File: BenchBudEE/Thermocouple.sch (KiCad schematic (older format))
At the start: 14 parts

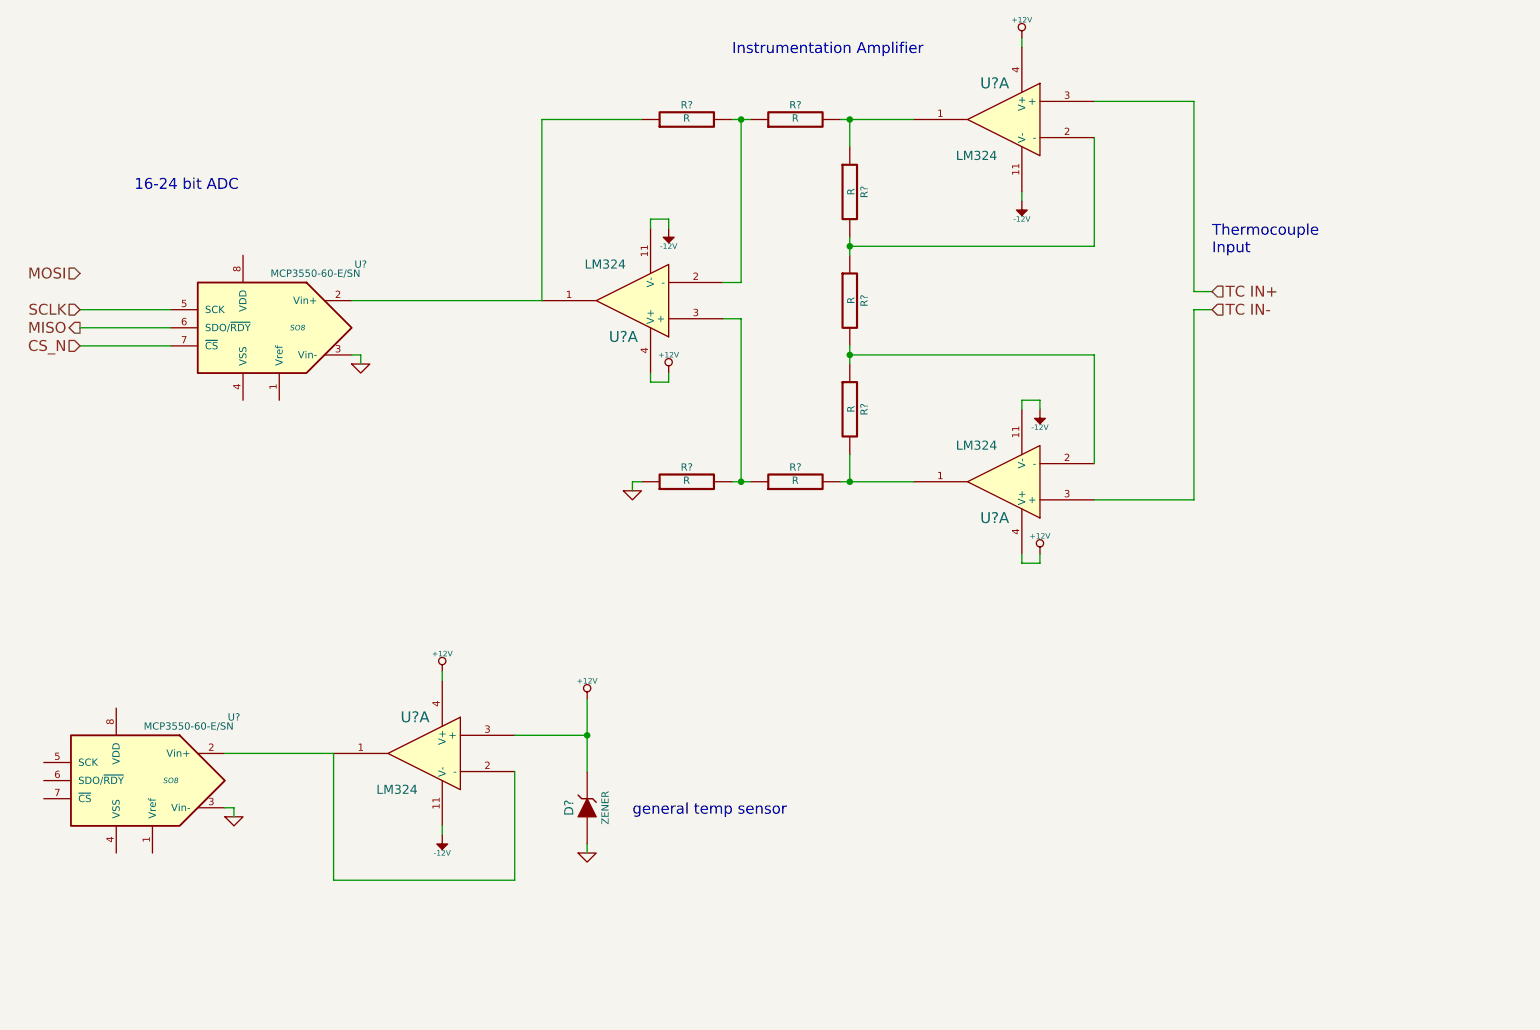
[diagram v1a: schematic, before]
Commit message: Completing schematics from week 3 videos.
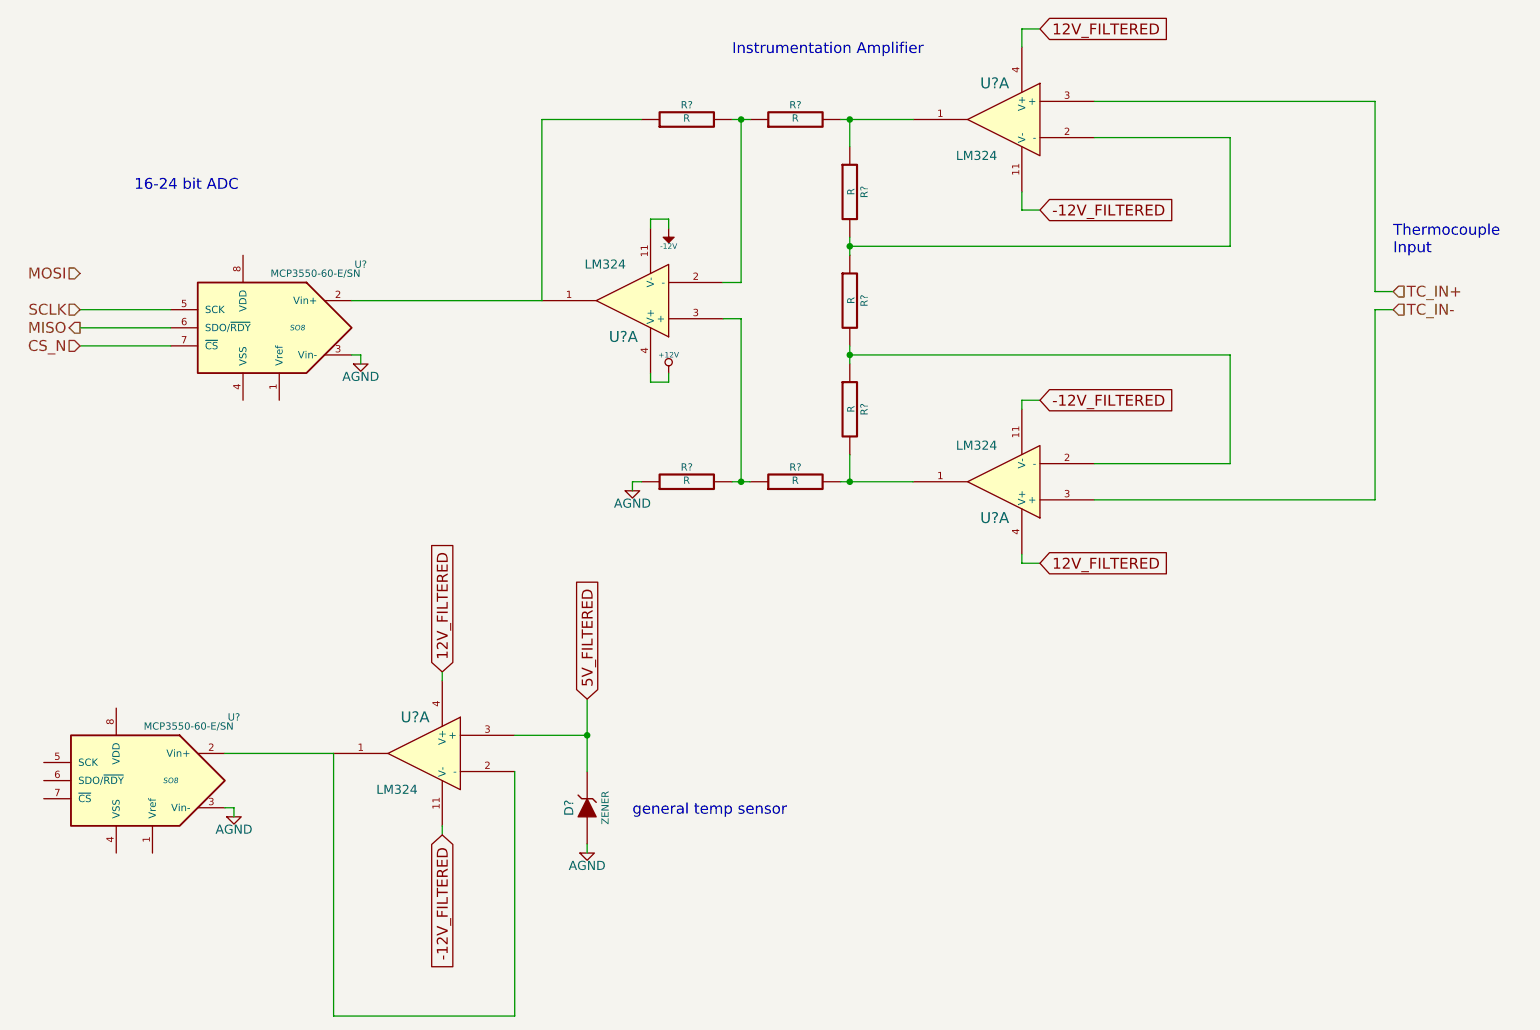
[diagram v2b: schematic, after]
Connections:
- net +12V: no longer D?.2 (K), U?.3 (+), U?.4 (V+), U?.4 (V+), U?.4 (V+)
- net -12V: no longer U?.11 (V-), U?.11 (V-), U?.11 (V-)
- net GND renamed AGND
- net TC IN+ renamed TC_IN+
- net TC IN- renamed TC_IN-
- new net -12V_FILTERED: U?.11 (V-), U?.11 (V-), U?.11 (V-)
- new net 12V_FILTERED: U?.4 (V+), U?.4 (V+), U?.4 (V+)
- new net 5V_FILTERED: D?.2 (K), U?.3 (+)
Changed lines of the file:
@@
 LIBS:relay_spdt
 LIBS:5566-20A
+LIBS:AP5726
+LIBS:arduino
 LIBS:BenchBudEE-cache
 EELAYER 27 0
@@
 $Descr A4 11693 8268
 encoding utf-8
-Sheet 3 9
+Sheet 2 9
 Title ""
-Date "13 feb 2014"
+Date "24 feb 2014"
 Rev ""
 Comp ""
@@
 Comment4 ""
 $EndDescr
-Text HLabel 8750 2750 2    60   Input ~ 0
-TC IN+
-Text HLabel 8750 2850 2    60   Input ~ 0
-TC IN-
+Text HLabel 9750 2750 2    60   Input ~ 0
+TC_IN+
+Text HLabel 9750 2850 2    60   Input ~ 0
+TC_IN-
 Text HLabel 2500 2650 0    60   Input ~ 0
 MOSI
@@
 $Comp
 L LM324 U?
-U 1 1 52F7EF65
-P 7600 3800
-F 0 "U?" H 7650 4000 60  0000 C CNN
-F 1 "LM324" H 7750 3600 50  0000 C CNN
-F 2 "" H 7600 3800 60  0000 C CNN
-F 3 "" H 7600 3800 60  0000 C CNN
-	1    7600 3800
-	-1   0    0    1
-$EndComp
-$Comp
-L LM324 U?
 U 1 1 52F7EF74
 P 5550 2800
@@
 $EndComp
 $Comp
-L -12V #PWR?
-U 1 1 52F7F282
-P 7800 3400
-F 0 "#PWR?" H 7800 3530 20  0001 C CNN
-F 1 "-12V" H 7800 3500 30  0000 C CNN
-F 2 "" H 7800 3400 60  0000 C CNN
-F 3 "" H 7800 3400 60  0000 C CNN
-	1    7800 3400
-	-1   0    0    1
-$EndComp
-$Comp
-L -12V #PWR?
-U 1 1 52F7F291
-P 7700 2250
-F 0 "#PWR?" H 7700 2380 20  0001 C CNN
-F 1 "-12V" H 7700 2350 30  0000 C CNN
-F 2 "" H 7700 2250 60  0000 C CNN
-F 3 "" H 7700 2250 60  0000 C CNN
-	1    7700 2250
-	-1   0    0    1
-$EndComp
-$Comp
 L +12V #PWR?
 U 1 1 52F7F33B
@@
 F 3 "" H 5750 3200 60  0000 C CNN
 	1    5750 3200
-	1    0    0    -1
-$EndComp
-$Comp
-L +12V #PWR?
-U 1 1 52F7F34A
-P 7800 4200
-F 0 "#PWR?" H 7800 4150 20  0001 C CNN
-F 1 "+12V" H 7800 4300 30  0000 C CNN
-F 2 "" H 7800 4200 60  0000 C CNN
-F 3 "" H 7800 4200 60  0000 C CNN
-	1    7800 4200
-	1    0    0    -1
-$EndComp
-$Comp
-L +12V #PWR?
-U 1 1 52F7F359
-P 7700 1350
-F 0 "#PWR?" H 7700 1300 20  0001 C CNN
-F 1 "+12V" H 7700 1450 30  0000 C CNN
-F 2 "" H 7700 1350 60  0000 C CNN
-F 3 "" H 7700 1350 60  0000 C CNN
-	1    7700 1350
-	1    0    0    -1
-$EndComp
-$Comp
-L GND #PWR?
-U 1 1 52F7F3EE
-P 5550 3850
-F 0 "#PWR?" H 5550 3850 30  0001 C CNN
-F 1 "GND" H 5550 3780 30  0001 C CNN
-F 2 "" H 5550 3850 60  0000 C CNN
-F 3 "" H 5550 3850 60  0000 C CNN
-	1    5550 3850
 	1    0    0    -1
 $EndComp
@@
 $EndComp
 $Comp
-L GND #PWR?
-U 1 1 52F7F4AB
-P 4050 3150
-F 0 "#PWR?" H 4050 3150 30  0001 C CNN
-F 1 "GND" H 4050 3080 30  0001 C CNN
-F 2 "" H 4050 3150 60  0000 C CNN
-F 3 "" H 4050 3150 60  0000 C CNN
-	1    4050 3150
-	1    0    0    -1
-$EndComp
-$Comp
 L MCP3550-60-E/SN U?
 U 1 1 52F7F58D
@@
 	0    -1   -1   0
 $EndComp
-$Comp
-L GND #PWR?
-U 1 1 52F7F5D7
-P 5300 5850
-F 0 "#PWR?" H 5300 5850 30  0001 C CNN
-F 1 "GND" H 5300 5780 30  0001 C CNN
-F 2 "" H 5300 5850 60  0000 C CNN
-F 3 "" H 5300 5850 60  0000 C CNN
-	1    5300 5850
-	1    0    0    -1
-$EndComp
-$Comp
-L +12V #PWR?
-U 1 1 52F7F612
-P 5300 5000
-F 0 "#PWR?" H 5300 4950 20  0001 C CNN
-F 1 "+12V" H 5300 5100 30  0000 C CNN
-F 2 "" H 5300 5000 60  0000 C CNN
-F 3 "" H 5300 5000 60  0000 C CNN
-	1    5300 5000
-	1    0    0    -1
-$EndComp
-$Comp
-L +12V #PWR?
-U 1 1 52F7F627
-P 4500 4850
-F 0 "#PWR?" H 4500 4800 20  0001 C CNN
-F 1 "+12V" H 4500 4950 30  0000 C CNN
-F 2 "" H 4500 4850 60  0000 C CNN
-F 3 "" H 4500 4850 60  0000 C CNN
-	1    4500 4850
-	1    0    0    -1
-$EndComp
-$Comp
-L -12V #PWR?
-U 1 1 52F7F62D
-P 4500 5750
-F 0 "#PWR?" H 4500 5880 20  0001 C CNN
-F 1 "-12V" H 4500 5850 30  0000 C CNN
-F 2 "" H 4500 5750 60  0000 C CNN
-F 3 "" H 4500 5750 60  0000 C CNN
-	1    4500 5750
-	-1   0    0    1
-$EndComp
 Wire Wire Line
 	6750 2450 6750 2550
@@
 Wire Wire Line
 	6750 3800 6750 3650
-Wire Wire Line
-	6750 3100 8100 3100
-Wire Wire Line
-	8100 3100 8100 3700
 Connection ~ 6750 3100
 Wire Wire Line
-	6750 2500 8100 2500
-Wire Wire Line
-	8100 2500 8100 1900
+	6750 2500 8850 2500
 Connection ~ 6750 2500
 Wire Wire Line
-	8750 2750 8650 2750
-Wire Wire Line
-	8650 2750 8650 1700
-Wire Wire Line
-	8650 1700 8100 1700
-Wire Wire Line
-	8750 2850 8650 2850
-Wire Wire Line
-	8650 2850 8650 3900
-Wire Wire Line
-	8650 3900 8100 3900
+	9750 2750 9650 2750
+Wire Wire Line
+	9650 2750 9650 1700
+Wire Wire Line
+	9650 1700 8100 1700
+Wire Wire Line
+	9750 2850 9650 2850
+Wire Wire Line
+	9650 2850 9650 3900
+Wire Wire Line
+	9650 3900 8100 3900
 Connection ~ 6750 1800
 Connection ~ 6750 3800
@@
 	5750 2350 5750 2400
 Wire Wire Line
-	7700 2200 7700 2250
-Wire Wire Line
 	7700 3400 7700 3350
 Wire Wire Line
 	7700 3350 7800 3350
 Wire Wire Line
-	7800 3350 7800 3400
-Wire Wire Line
-	7700 1350 7700 1400
+	7700 1300 7700 1400
 Wire Wire Line
 	7700 4200 7700 4250
@@
 	7700 4250 7800 4250
 Wire Wire Line
-	7800 4250 7800 4200
-Wire Wire Line
 	5650 3200 5650 3250
 Wire Wire Line
@@
 	5300 5000 5300 5400
 Wire Wire Line
-	3900 5300 3900 6000
-Wire Wire Line
-	3900 6000 4900 6000
-Wire Wire Line
-	4900 6000 4900 5400
+	3900 5300 3900 6750
+Wire Wire Line
+	4900 5400 4900 6750
 Wire Wire Line
 	4900 5200 5300 5200
@@
 Wire Wire Line
 	3900 5300 3300 5300
-$Comp
-L GND #PWR?
-U 1 1 52F7F813
-P 3350 5650
-F 0 "#PWR?" H 3350 5650 30  0001 C CNN
-F 1 "GND" H 3350 5580 30  0001 C CNN
-F 2 "" H 3350 5650 60  0000 C CNN
-F 3 "" H 3350 5650 60  0000 C CNN
-	1    3350 5650
-	1    0    0    -1
-$EndComp
 Wire Wire Line
 	3300 5600 3350 5600
@@
 Text Notes 5550 5650 0    60   ~ 0
 general temp sensor
-Text Notes 8750 2550 0    60   ~ 0
+Text Notes 9750 2550 0    60   ~ 0
 Thermocouple\nInput
 Text Notes 6100 1450 0    60   ~ 0
@@
 Text Notes 2800 2200 0    60   ~ 0
 16-24 bit ADC
+$Comp
+L AGND #PWR?
+U 1 1 53098A6F
+P 3350 5650
+F 0 "#PWR?" H 3350 5650 40  0001 C CNN
+F 1 "AGND" H 3350 5580 50  0000 C CNN
+F 2 "" H 3350 5650 60  0000 C CNN
+F 3 "" H 3350 5650 60  0000 C CNN
+	1    3350 5650
+	1    0    0    -1
+$EndComp
+$Comp
+L AGND #PWR?
+U 1 1 53098A7E
+P 5300 5850
+F 0 "#PWR?" H 5300 5850 40  0001 C CNN
+F 1 "AGND" H 5300 5780 50  0000 C CNN
+F 2 "" H 5300 5850 60  0000 C CNN
+F 3 "" H 5300 5850 60  0000 C CNN
+	1    5300 5850
+	1    0    0    -1
+$EndComp
+Text GLabel 5300 5000 1    60   Input ~ 0
+5V_FILTERED
+Text GLabel 4500 4850 1    60   Input ~ 0
+12V_FILTERED
+Text GLabel 4500 5750 3    60   Input ~ 0
+-12V_FILTERED
+Wire Wire Line
+	4900 6750 3900 6750
+$Comp
+L LM324 U?
+U 1 1 52F7EF65
+P 7600 3800
+F 0 "U?" H 7650 4000 60  0000 C CNN
+F 1 "LM324" H 7750 3600 50  0000 C CNN
+F 2 "" H 7600 3800 60  0000 C CNN
+F 3 "" H 7600 3800 60  0000 C CNN
+	1    7600 3800
+	-1   0    0    1
+$EndComp
+Text GLabel 7800 4250 2    60   Input ~ 0
+12V_FILTERED
+$Comp
+L AGND #PWR?
+U 1 1 53098ACE
+P 5550 3850
+F 0 "#PWR?" H 5550 3850 40  0001 C CNN
+F 1 "AGND" H 5550 3780 50  0000 C CNN
+F 2 "" H 5550 3850 60  0000 C CNN
+F 3 "" H 5550 3850 60  0000 C CNN
+	1    5550 3850
+	1    0    0    -1
+$EndComp
+$Comp
+L AGND #PWR?
+U 1 1 53098ADD
+P 4050 3150
+F 0 "#PWR?" H 4050 3150 40  0001 C CNN
+F 1 "AGND" H 4050 3080 50  0000 C CNN
+F 2 "" H 4050 3150 60  0000 C CNN
+F 3 "" H 4050 3150 60  0000 C CNN
+	1    4050 3150
+	1    0    0    -1
+$EndComp
+Text GLabel 7800 3350 2    60   Input ~ 0
+-12V_FILTERED
+Text GLabel 7800 2300 2    60   Input ~ 0
+-12V_FILTERED
+Wire Wire Line
+	7800 2300 7700 2300
+Wire Wire Line
+	7700 2300 7700 2200
+Wire Wire Line
+	8100 1900 8850 1900
+Wire Wire Line
+	8850 1900 8850 2500
+Wire Wire Line
+	8100 3700 8850 3700
+Wire Wire Line
+	8850 3700 8850 3100
+Wire Wire Line
+	8850 3100 6750 3100
+Text GLabel 7800 1300 2    60   Input ~ 0
+12V_FILTERED
+Wire Wire Line
+	7800 1300 7700 1300
 $EndSCHEMATC

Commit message: checking in all my local changes before syncing to chris's repo.
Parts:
- gave numbers to parts that had none: 11
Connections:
- net TC_IN+: now also U4.10 (+); no longer U4.3 (+)
- net TC_IN-: now also U4.12 (+); no longer U4.3 (+)
- net at R10.1, R8.2: now also U4.8; no longer U4.1
- net at R10.2, R11.1: now also U4.9 (-); no longer U4.2 (-)
- net at R12.2, R9.2: now also U4.14; no longer U4.1
- net at R11.2, R12.1: now also U4.13 (-); no longer U4.2 (-)
- net at R6.1, U3.2 (Vin+): now also U4.7; no longer U4.1
- net at R6.2, R8.1: now also U4.6 (-); no longer U4.2 (-)
- net at R7.2, R9.1: now also U4.5 (+); no longer U4.3 (+)
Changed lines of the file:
@@
 Sheet 2 9
 Title ""
-Date "24 feb 2014"
+Date "2 mar 2014"
 Rev ""
 Comp ""
@@
 CS_N
 $Comp
-L LM324 U?
-U 1 1 52F7EF56
+L LM324 U4
+U 3 1 52F7EF56
 P 7600 1800
-F 0 "U?" H 7650 2000 60  0000 C CNN
+F 0 "U4" H 7650 2000 60  0000 C CNN
 F 1 "LM324" H 7750 1600 50  0000 C CNN
 F 2 "" H 7600 1800 60  0000 C CNN
 F 3 "" H 7600 1800 60  0000 C CNN
-	1    7600 1800
+	3    7600 1800
 	-1   0    0    -1
 $EndComp
 $Comp
-L LM324 U?
-U 1 1 52F7EF74
+L LM324 U4
+U 2 1 52F7EF74
 P 5550 2800
-F 0 "U?" H 5600 3000 60  0000 C CNN
+F 0 "U4" H 5600 3000 60  0000 C CNN
 F 1 "LM324" H 5700 2600 50  0000 C CNN
 F 2 "" H 5550 2800 60  0000 C CNN
 F 3 "" H 5550 2800 60  0000 C CNN
-	1    5550 2800
+	2    5550 2800
 	-1   0    0    1
 $EndComp
 $Comp
-L LM324 U?
+L LM324 U4
 U 1 1 52F7EF83
 P 4400 5300
-F 0 "U?" H 4450 5500 60  0000 C CNN
+F 0 "U4" H 4450 5500 60  0000 C CNN
 F 1 "LM324" H 4550 5100 50  0000 C CNN
 F 2 "" H 4400 5300 60  0000 C CNN
@@
 $EndComp
 $Comp
-L R R?
+L R R11
 U 1 1 52F7EF92
 P 6750 2800
-F 0 "R?" V 6830 2800 40  0000 C CNN
+F 0 "R11" V 6830 2800 40  0000 C CNN
 F 1 "R" V 6757 2801 40  0000 C CNN
 F 2 "~" V 6680 2800 30  0000 C CNN
@@
 $EndComp
 $Comp
-L R R?
+L R R10
 U 1 1 52F7EFBD
 P 6750 2200
-F 0 "R?" V 6830 2200 40  0000 C CNN
+F 0 "R10" V 6830 2200 40  0000 C CNN
 F 1 "R" V 6757 2201 40  0000 C CNN
 F 2 "~" V 6680 2200 30  0000 C CNN
@@
 $EndComp
 $Comp
-L R R?
+L R R12
 U 1 1 52F7EFC3
 P 6750 3400
-F 0 "R?" V 6830 3400 40  0000 C CNN
+F 0 "R12" V 6830 3400 40  0000 C CNN
 F 1 "R" V 6757 3401 40  0000 C CNN
 F 2 "~" V 6680 3400 30  0000 C CNN
@@
 $EndComp
 $Comp
-L R R?
+L R R9
 U 1 1 52F7F036
 P 6450 3800
-F 0 "R?" V 6530 3800 40  0000 C CNN
+F 0 "R9" V 6530 3800 40  0000 C CNN
 F 1 "R" V 6457 3801 40  0000 C CNN
 F 2 "~" V 6380 3800 30  0000 C CNN
@@
 $EndComp
 $Comp
-L R R?
+L R R8
 U 1 1 52F7F03C
 P 6450 1800
-F 0 "R?" V 6530 1800 40  0000 C CNN
+F 0 "R8" V 6530 1800 40  0000 C CNN
 F 1 "R" V 6457 1801 40  0000 C CNN
 F 2 "~" V 6380 1800 30  0000 C CNN
@@
 $EndComp
 $Comp
-L R R?
+L R R6
 U 1 1 52F7F069
 P 5850 1800
-F 0 "R?" V 5930 1800 40  0000 C CNN
+F 0 "R6" V 5930 1800 40  0000 C CNN
 F 1 "R" V 5857 1801 40  0000 C CNN
 F 2 "~" V 5780 1800 30  0000 C CNN
@@
 $EndComp
 $Comp
-L R R?
+L R R7
 U 1 1 52F7F06F
 P 5850 3800
-F 0 "R?" V 5930 3800 40  0000 C CNN
+F 0 "R7" V 5930 3800 40  0000 C CNN
 F 1 "R" V 5857 3801 40  0000 C CNN
 F 2 "~" V 5780 3800 30  0000 C CNN
@@
 $EndComp
 $Comp
-L -12V #PWR?
+L -12V #PWR5
 U 1 1 52F7F273
 P 5750 2400
-F 0 "#PWR?" H 5750 2530 20  0001 C CNN
+F 0 "#PWR5" H 5750 2530 20  0001 C CNN
 F 1 "-12V" H 5750 2500 30  0000 C CNN
 F 2 "" H 5750 2400 60  0000 C CNN
@@
 $EndComp
 $Comp
-L +12V #PWR?
+L +12V #PWR6
 U 1 1 52F7F33B
 P 5750 3200
-F 0 "#PWR?" H 5750 3150 20  0001 C CNN
+F 0 "#PWR6" H 5750 3150 20  0001 C CNN
 F 1 "+12V" H 5750 3300 30  0000 C CNN
 F 2 "" H 5750 3200 60  0000 C CNN
@@
 $EndComp
 $Comp
-L MCP3550-60-E/SN U?
+L MCP3550-60-E/SN U3
 U 1 1 52F7F458
 P 3500 2950
-F 0 "U?" H 2950 3300 40  0000 C CNN
+F 0 "U3" H 2950 3300 40  0000 C CNN
 F 1 "MCP3550-60-E/SN" H 3200 3250 40  0000 C CNN
 F 2 "SO8" H 3300 2950 30  0000 C CIN
@@
 $EndComp
 $Comp
-L MCP3550-60-E/SN U?
+L MCP3550-60-E/SN U2
 U 1 1 52F7F58D
 P 2800 5450
-F 0 "U?" H 2250 5800 40  0000 C CNN
+F 0 "U2" H 2250 5800 40  0000 C CNN
 F 1 "MCP3550-60-E/SN" H 2500 5750 40  0000 C CNN
 F 2 "SO8" H 2600 5450 30  0000 C CIN
@@
 $EndComp
 $Comp
-L ZENER D?
+L ZENER D3
 U 1 1 52F7F5CA
 P 5300 5600
-F 0 "D?" H 5300 5700 50  0000 C CNN
+F 0 "D3" H 5300 5700 50  0000 C CNN
 F 1 "ZENER" H 5300 5500 40  0000 C CNN
 F 2 "~" H 5300 5600 60  0000 C CNN
@@
 16-24 bit ADC
 $Comp
-L AGND #PWR?
+L AGND #PWR1
 U 1 1 53098A6F
 P 3350 5650
-F 0 "#PWR?" H 3350 5650 40  0001 C CNN
+F 0 "#PWR1" H 3350 5650 40  0001 C CNN
 F 1 "AGND" H 3350 5580 50  0000 C CNN
 F 2 "" H 3350 5650 60  0000 C CNN
@@
 $EndComp
 $Comp
-L AGND #PWR?
+L AGND #PWR3
 U 1 1 53098A7E
 P 5300 5850
-F 0 "#PWR?" H 5300 5850 40  0001 C CNN
+F 0 "#PWR3" H 5300 5850 40  0001 C CNN
 F 1 "AGND" H 5300 5780 50  0000 C CNN
 F 2 "" H 5300 5850 60  0000 C CNN
@@
 	4900 6750 3900 6750
 $Comp
-L LM324 U?
-U 1 1 52F7EF65
+L LM324 U4
+U 4 1 52F7EF65
 P 7600 3800
-F 0 "U?" H 7650 4000 60  0000 C CNN
+F 0 "U4" H 7650 4000 60  0000 C CNN
 F 1 "LM324" H 7750 3600 50  0000 C CNN
 F 2 "" H 7600 3800 60  0000 C CNN
 F 3 "" H 7600 3800 60  0000 C CNN
-	1    7600 3800
+	4    7600 3800
 	-1   0    0    1
 $EndComp
@@
 12V_FILTERED
 $Comp
-L AGND #PWR?
+L AGND #PWR4
 U 1 1 53098ACE
 P 5550 3850
-F 0 "#PWR?" H 5550 3850 40  0001 C CNN
+F 0 "#PWR4" H 5550 3850 40  0001 C CNN
 F 1 "AGND" H 5550 3780 50  0000 C CNN
 F 2 "" H 5550 3850 60  0000 C CNN
@@
 $EndComp
 $Comp
-L AGND #PWR?
+L AGND #PWR2
 U 1 1 53098ADD
 P 4050 3150
-F 0 "#PWR?" H 4050 3150 40  0001 C CNN
+F 0 "#PWR2" H 4050 3150 40  0001 C CNN
 F 1 "AGND" H 4050 3080 50  0000 C CNN
 F 2 "" H 4050 3150 60  0000 C CNN
